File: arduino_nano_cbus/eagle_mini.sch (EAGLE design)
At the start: 28 parts, among them J1 1X2-3.5MM, J2 1X2-3.5MM, M1 ARDUINO-PRO-MINI-5.0V

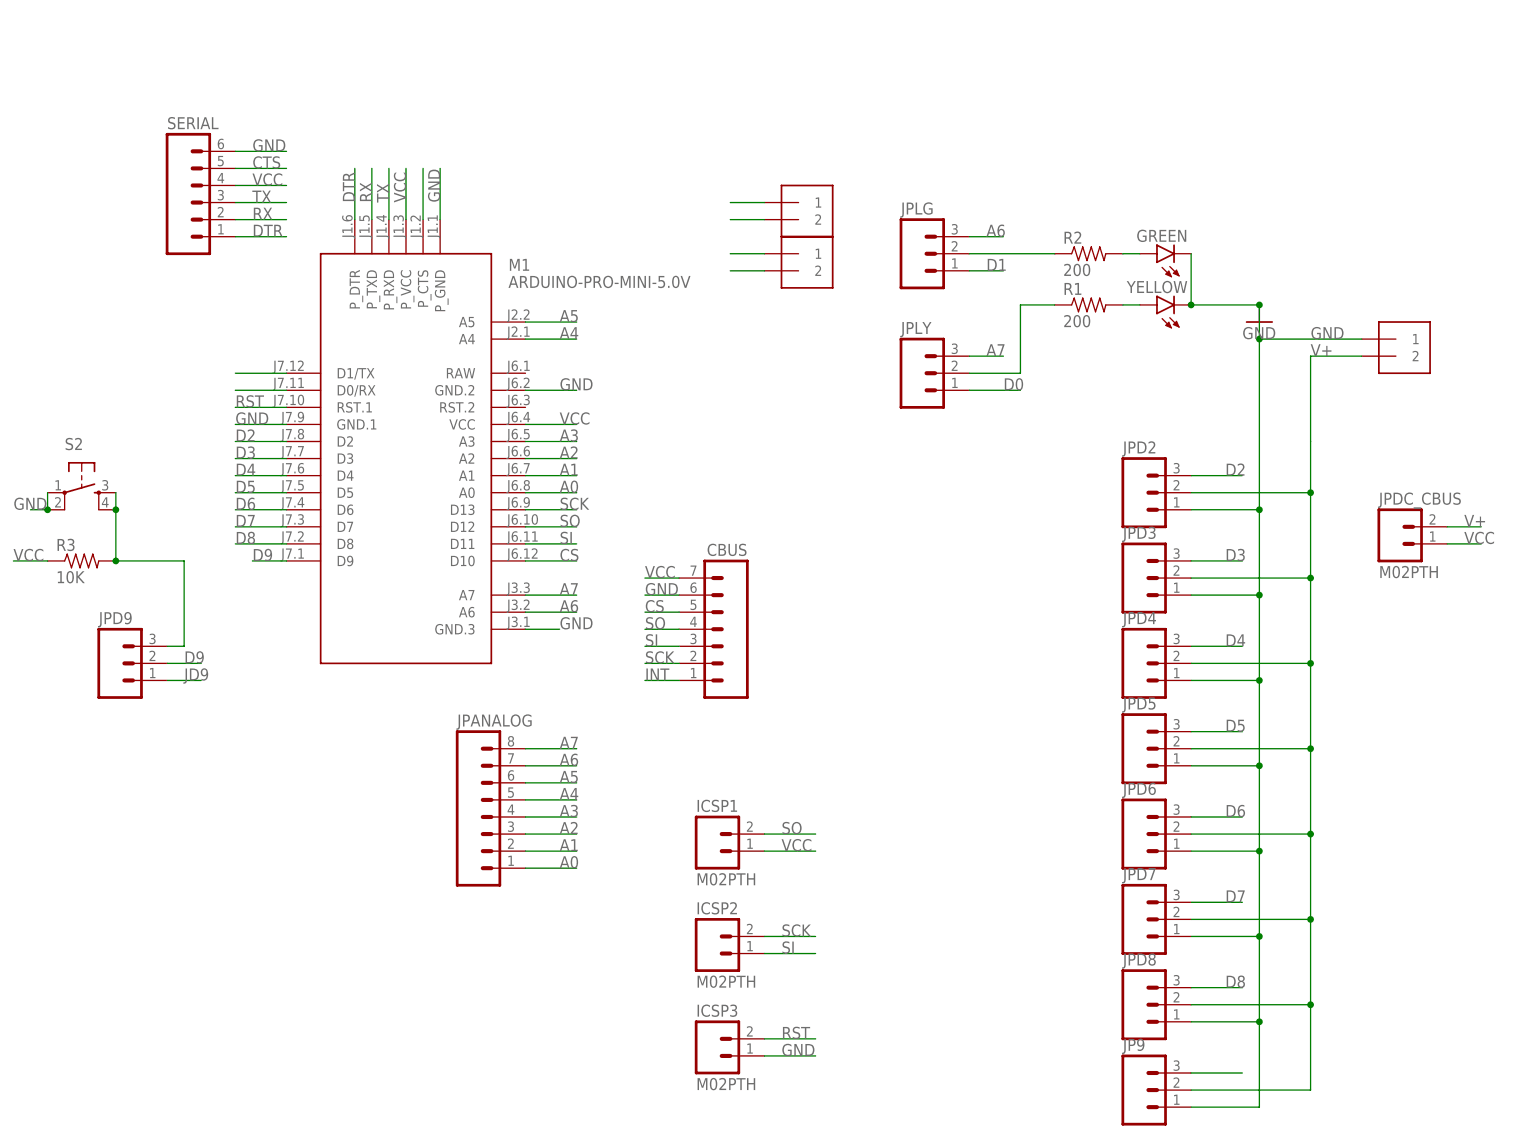
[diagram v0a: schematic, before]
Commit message: car shield with atmega 328
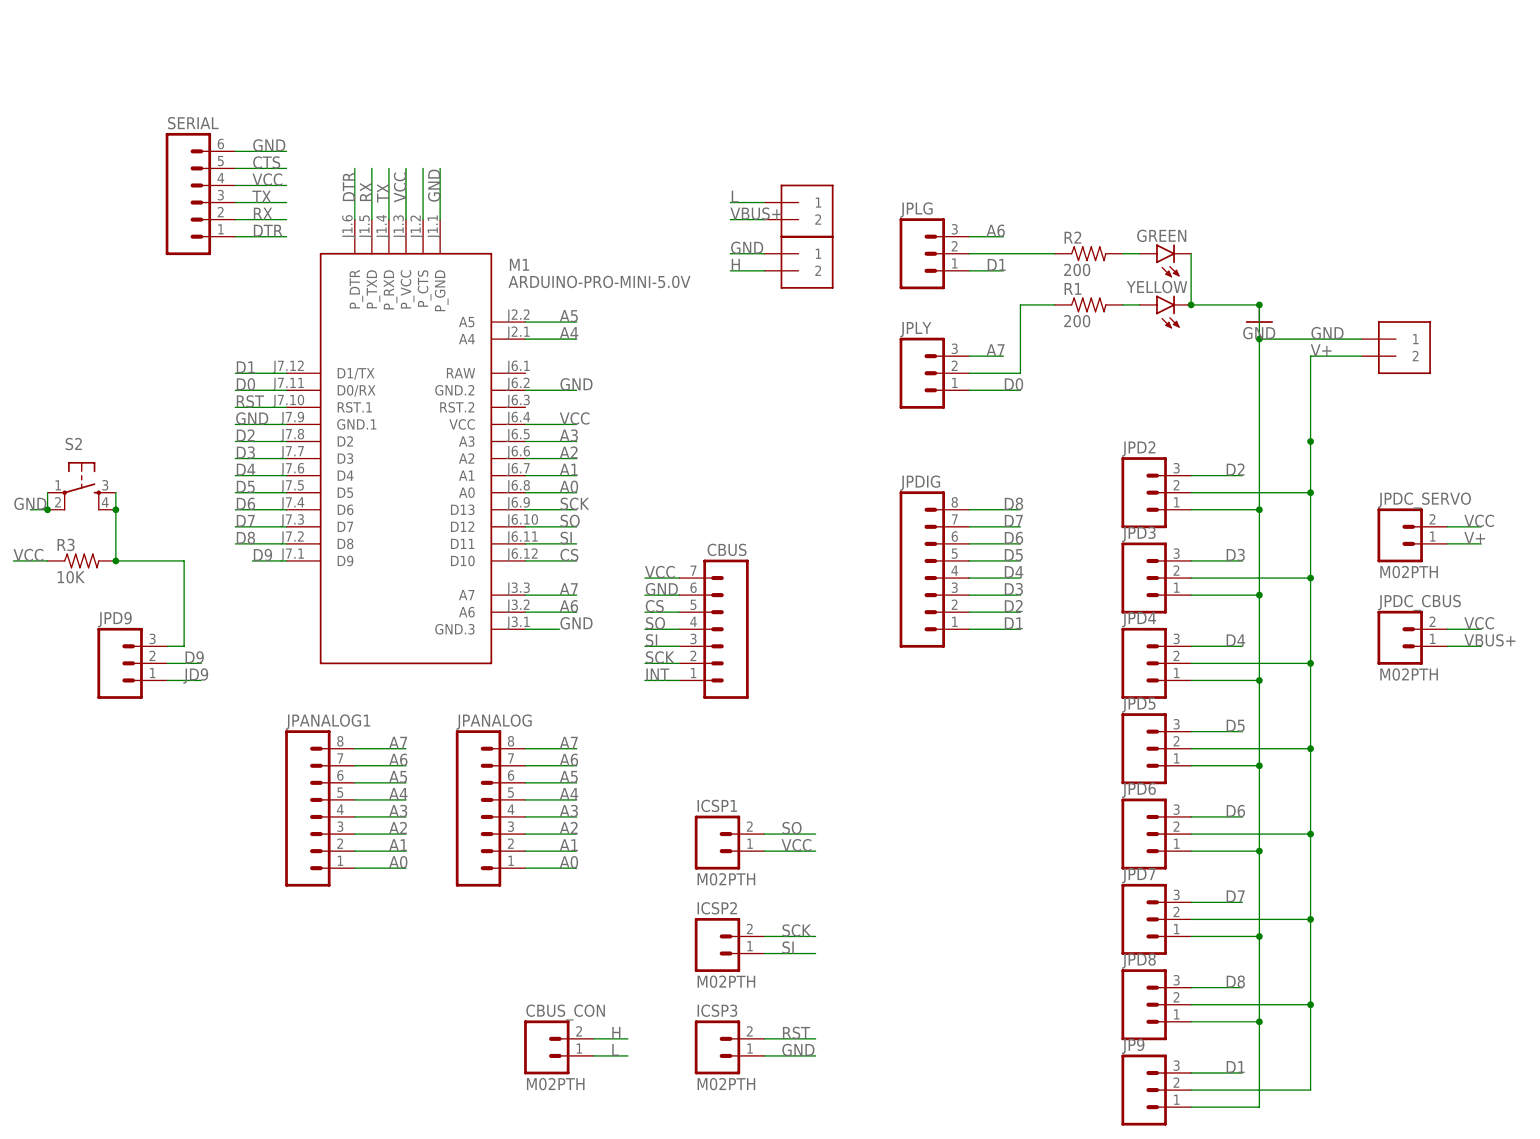
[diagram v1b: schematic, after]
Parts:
- added CBUS_CON, JPDC_SERVO: M02PTH, SparkFun-Connectors:M02PTH
- added JPANALOG1, JPDIG: (no value), SparkFun-Connectors:M08
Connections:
- removed net N$1: J2.2
- removed net N$15: J1.1
- removed net N$16: J1.2
- removed net N$3: J2.1
- removed net N$4: JP9.2, JPD2.2, JPD3.2, JPD4.2, JPD5.2, JPD6.2, JPD7.2, JPD8.2
- new net H: CBUS_CON.2, J1.2
- new net L: CBUS_CON.1, J2.1
- new net VBUS+: J2.2, JPDC_CBUS.1
- net A0: now also JPANALOG1.1
- net A1: now also JPANALOG1.2
- net A2: now also JPANALOG1.3
- net A3: now also JPANALOG1.4
- net A4: now also JPANALOG1.5
- net A5: now also JPANALOG1.6
- net A6: now also JPANALOG1.7
- net A7: now also JPANALOG1.8
- net D1: now also JP9.3, JPDIG.1
- net D2: now also JPDIG.2
- net D3: now also JPDIG.3
- net D4: now also JPDIG.4
- net D5: now also JPDIG.5
- net D6: now also JPDIG.6
- net D7: now also JPDIG.7
- net D8: now also JPDIG.8
- net GND: now also J1.1
- net JD9: no longer JP9.3
- net V+: now also JP9.2, JPD2.2, JPD3.2, JPD4.2, JPD5.2, JPD6.2, JPD7.2, JPD8.2, JPDC_SERVO.1; no longer JPDC_CBUS.2
- net VCC: now also JPDC_CBUS.2, JPDC_SERVO.2; no longer JPDC_CBUS.1
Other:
- moved on the sheet: JPDC_CBUS

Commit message: some improvement on the boards.
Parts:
- added C1, C2: 100uF, adafruit:CPOL-USE2.5-6
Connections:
- net GND: now also C1.-, C2.-
- net VCC: now also C1.+, C2.+
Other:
- moved on the sheet: CBUS, CBUS_CON, JPDIG, SERIAL

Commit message: bug fixes and better board routing
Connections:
- net A0: now also JPLG.3
- net A1: now also JPLY.3
- net A6: no longer JPLG.3
- net A7: no longer JPLY.3
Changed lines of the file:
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@@
 <net name="GND" class="0">
-<segment>
-<pinref part="CBUS" gate="G$1" pin="6"/>
-<label x="68.58" y="40.64" size="1.778" layer="95"/>
-<wire x1="58.42" y1="38.1" x2="63.5" y2="38.1" width="0.1524" layer="91"/>
-<wire x1="63.5" y1="38.1" x2="63.5" y2="40.64" width="0.1524" layer="91"/>
-<wire x1="63.5" y1="40.64" x2="73.66" y2="40.64" width="0.1524" layer="91"/>
-<pinref part="C1" gate="G$1" pin="-"/>
-</segment>
 <segment>
 <pinref part="GREEN" gate="G$1" pin="C"/>
@@
 <segment>
 <pinref part="M1" gate="G$1" pin="GND.3"/>
-<wire x1="38.1" y1="17.78" x2="43.18" y2="17.78" width="0.1524" layer="91"/>
 <label x="43.18" y="17.78" size="1.778" layer="95"/>
+<pinref part="CBUS" gate="G$1" pin="6"/>
+<label x="68.58" y="40.64" size="1.778" layer="95"/>
+<wire x1="58.42" y1="38.1" x2="60.96" y2="38.1" width="0.1524" layer="91"/>
+<wire x1="60.96" y1="38.1" x2="63.5" y2="38.1" width="0.1524" layer="91"/>
+<wire x1="63.5" y1="38.1" x2="63.5" y2="40.64" width="0.1524" layer="91"/>
+<wire x1="63.5" y1="40.64" x2="73.66" y2="40.64" width="0.1524" layer="91"/>
+<pinref part="C1" gate="G$1" pin="-"/>
+<wire x1="38.1" y1="17.78" x2="60.96" y2="17.78" width="0.1524" layer="91"/>
+<wire x1="60.96" y1="17.78" x2="60.96" y2="38.1" width="0.1524" layer="91"/>
+<junction x="60.96" y="38.1"/>
 </segment>
 <segment>
@@
 <label x="17.78" y="-17.78" size="1.778" layer="95"/>
 </segment>
+<segment>
+<pinref part="JPLG" gate="G$1" pin="3"/>
+<wire x1="104.14" y1="76.2" x2="109.22" y2="76.2" width="0.1524" layer="91"/>
+<label x="106.68" y="76.2" size="1.778" layer="95"/>
+</segment>
 </net>
 <net name="A1" class="0">
@@
 <label x="17.78" y="-15.24" size="1.778" layer="95"/>
 </segment>
+<segment>
+<pinref part="JPLY" gate="G$1" pin="3"/>
+<wire x1="104.14" y1="58.42" x2="109.22" y2="58.42" width="0.1524" layer="91"/>
+<label x="106.68" y="58.42" size="1.778" layer="95"/>
+</segment>
 </net>
 <net name="A2" class="0">
@@
 </segment>
 <segment>
-<pinref part="JPLG" gate="G$1" pin="3"/>
-<wire x1="104.14" y1="76.2" x2="109.22" y2="76.2" width="0.1524" layer="91"/>
-<label x="106.68" y="76.2" size="1.778" layer="95"/>
-</segment>
-<segment>
 <pinref part="JPANALOG1" gate="G$1" pin="7"/>
 <wire x1="12.7" y1="-2.54" x2="20.32" y2="-2.54" width="0.1524" layer="91"/>
@@
 </segment>
 <segment>
-<pinref part="JPLY" gate="G$1" pin="3"/>
-<wire x1="104.14" y1="58.42" x2="109.22" y2="58.42" width="0.1524" layer="91"/>
-<label x="106.68" y="58.42" size="1.778" layer="95"/>
-</segment>
-<segment>
